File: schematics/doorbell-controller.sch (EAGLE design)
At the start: 17 parts, among them Q1 BC557

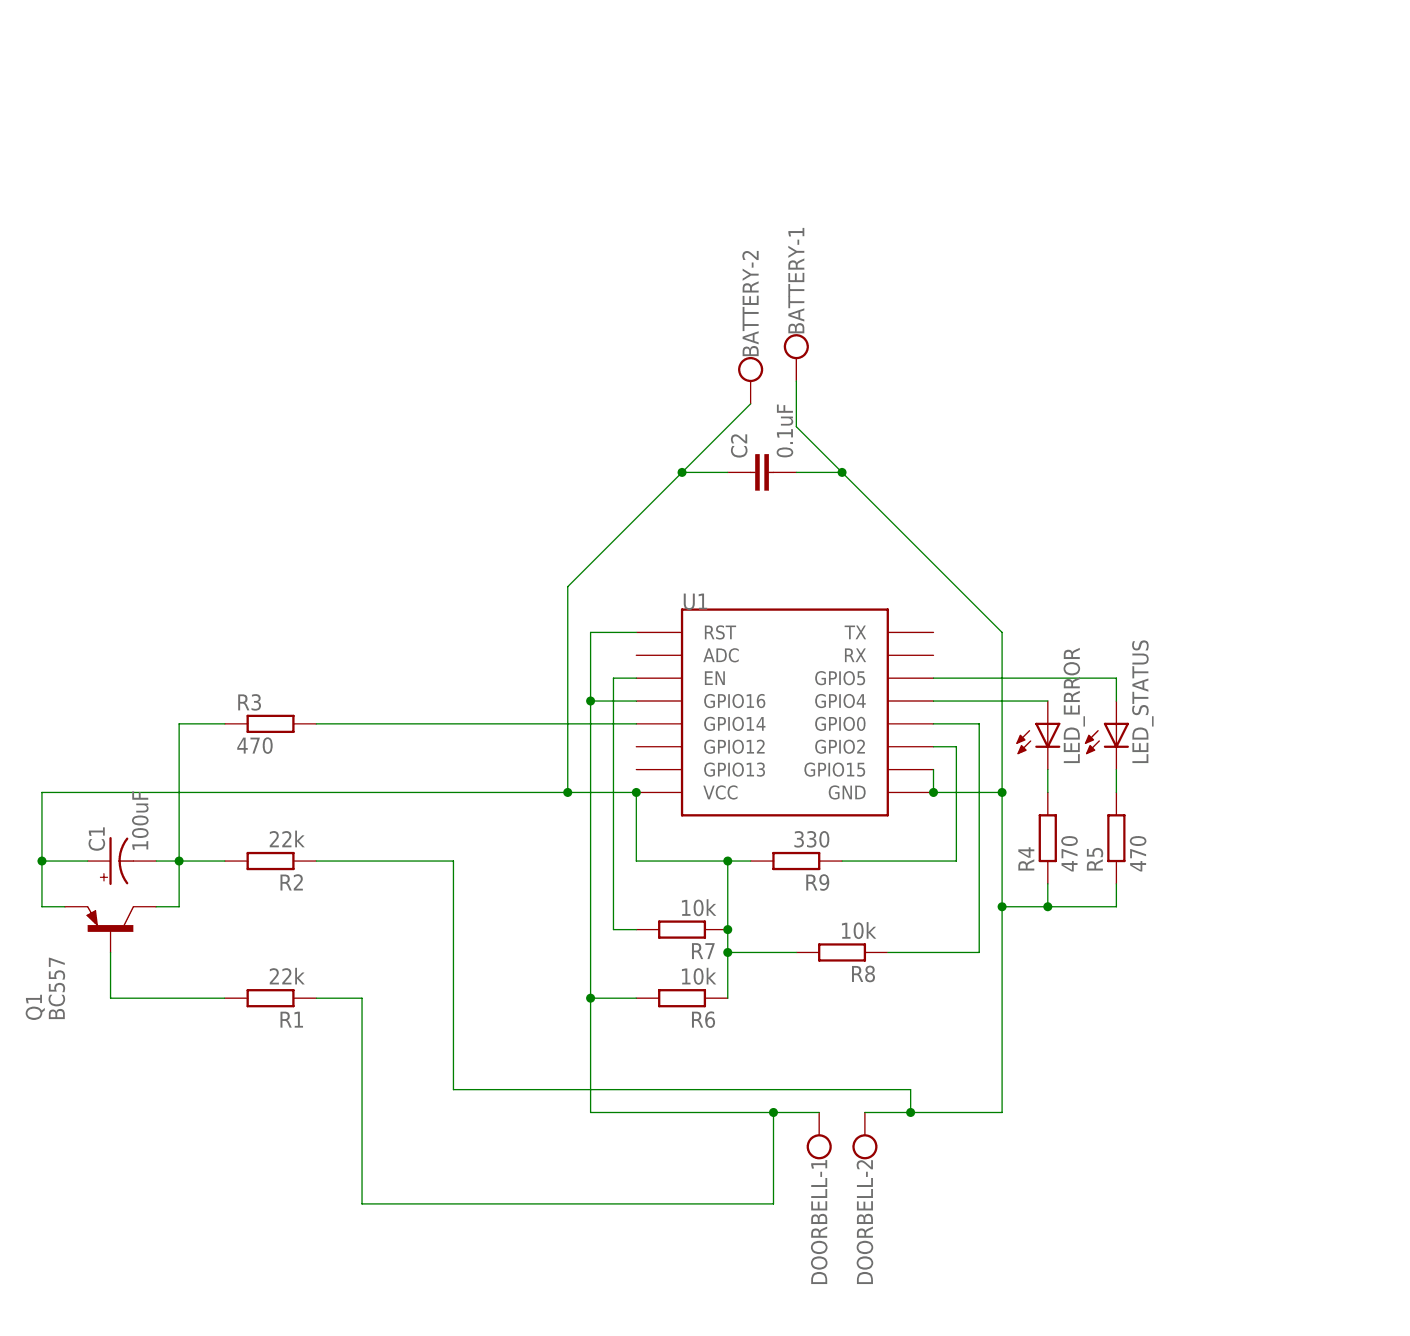
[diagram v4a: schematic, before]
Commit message: Added voltage regulator to schematics
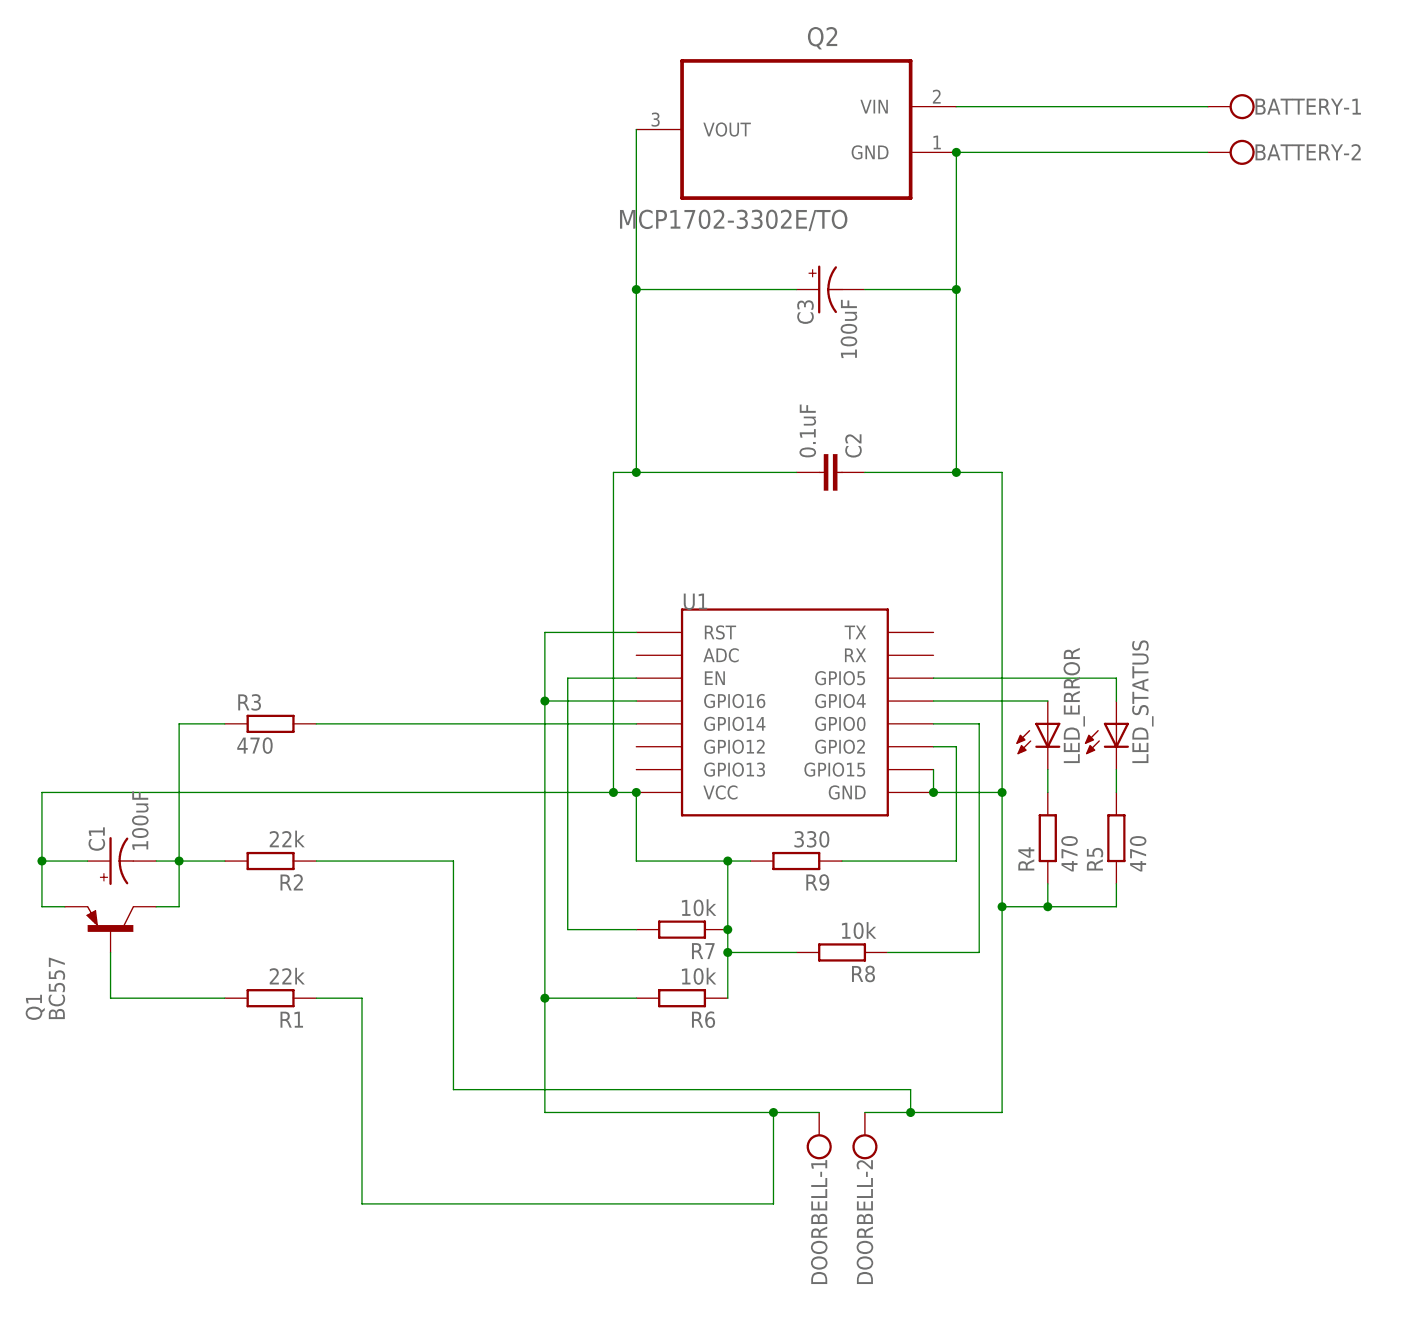
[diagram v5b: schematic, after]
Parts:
- added C3: 100uF, rcl:CPOL-USE2,5-6E
- added Q2: MCP1702-3302E/TO, Microchip_By_element14_Batch_1:MCP1702-3302E/TO
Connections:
- removed net N$8: BATTERY-2.KL, C1.+, C2.1, Q1.E, R6.1, R7.1, R8.2, R9.2, U1.VCC
- new net BATT_VIN: BATTERY-1.KL, Q2.VIN
- new net VCC: C1.+, C2.2, C3.+, Q1.E, Q2.VOUT, R6.1, R7.1, R8.2, R9.2, U1.VCC
- net GND: now also BATTERY-2.KL, C2.1, C3.-, Q2.GND; no longer BATTERY-1.KL, C2.2
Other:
- moved on the sheet: BATTERY-1, BATTERY-2, C2
